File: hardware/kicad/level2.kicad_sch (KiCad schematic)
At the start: 13 parts, among them J1 19V in (switched, fused), J3 motor: A1 A2 B1 B2, J4 to ESP32: STEP DIR EN HALL 3V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, J5 to Hall: 5V GND OUT, J6 to buck: 19V, GND, 5V, M1 NEMA17 (42 x 33.4), U1 BTT TMC2209, U3 ESP32-S3-DevKitC-1 N16R8, U4 A3144 (homing)

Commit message: Perfboard layout: parts on the hole grid, routed wires, wiring picture (perfboard_wiring.png); schematic gets footprints
Co-Authored-By: Claude Opus 5.5 <noreply@anthropic.com>
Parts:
- C1, C2: footprint (none) -> Capacitor_THT:CP_Radial_D8.0mm_P5.00mm
- J1: footprint (none) -> TerminalBlock_Phoenix:TerminalBlock_Phoenix_MKDS-1,5-2-5.08_1x02_P5.08mm_Horizontal
- J3: footprint (none) -> TerminalBlock_Phoenix:TerminalBlock_Phoenix_MKDS-1,5-4-5.08_1x04_P5.08mm_Horizontal
- J4: footprint (none) -> Connector_PinHeader_2.54mm:PinHeader_1x06_P2.54mm_Vertical
- J5: footprint (none) -> Connector_PinHeader_2.54mm:PinHeader_1x03_P2.54mm_Vertical
- J6: footprint (none) -> TerminalBlock_Phoenix:TerminalBlock_Phoenix_MKDS-1,5-3-5.08_1x03_P5.08mm_Horizontal
- R1, R2: footprint (none) -> Resistor_THT:R_Axial_DIN0207_L6.3mm_D2.5mm_P10.16mm_Horizontal
- U1: footprint (none) -> Module:Pololu_Breakout-16_15.2x20.3mm

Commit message: Perfboard: driver turned under J3 (coil wires straight up, A2 A1 B1 B2), J1 + next to J6 19V, C1 above VS; C2 dropped
Co-Authored-By: Claude Opus 5.5 <noreply@anthropic.com>
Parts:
- removed C2: 100uF 50V (opt., at J1), Capacitor_THT:CP_Radial_D8.0mm_P5.00mm, symbol Device:C_Polarized
- J1: value 19V in (switched, fused) -> 19V in: + - left to right
- J3: value motor: A1 A2 B1 B2 -> motor: A2 A1 B1 B2 (left to right on the board)
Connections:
- net +19V_SW: now also J1.2 (Pin_2); no longer J1.1 (Pin_1)
- net GND: now also J1.1 (Pin_1); no longer J1.2 (Pin_2)
- net MOT_A1: now also J3.3 (Pin_3); no longer J3.1 (Pin_1)
- net MOT_A2: now also J3.4 (Pin_4); no longer J3.2 (Pin_2)
- net MOT_B1: now also J3.2 (Pin_2); no longer J3.3 (Pin_3)
- net MOT_B2: now also J3.1 (Pin_1); no longer J3.4 (Pin_4)
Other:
- note added: "Heavy wire (20-22 AWG): 19 V, GND, motor. C1 sits right at U1's VS and the GND next to it."
- note added: "Motor M1: 6-pin socket, pins 1+3 = coil A (red A1, blue A2); pins 4+6 = coil B (green B1, black B2); pins 2, 5 (centre taps) unused. J3 left to right: A2 A1 B1 B2."
- note removed: "Heavy wire (20-22 AWG): 19 V, GND, motor. C1 sits right at U1's VS and the GND next to it; C2 (optional) at J1."
- note removed: "Motor M1: 6-pin socket, pins 1+3 = coil A (red, blue) -> A1, A2; pins 4+6 = coil B (green, black) -> B1, B2; pins 2, 5 (centre taps) unused."
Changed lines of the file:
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@@
 (symbol (lib_id "Connector:Screw_Terminal_01x02") (at 63.5 50.8 0) (unit 1) (exclude_from_sim no) (in_bom yes) (on_board yes) (dnp no)
 (property "Reference" "J1" (at 63.5 48.26 0) (effects (font (size 1.27 1.27))))
-(property "Value" "19V in (switched, fused)" (at 63.5 55.88 0) (effects (font (size 1.27 1.27))))
+(property "Value" "19V in: + - left to right" (at 63.5 55.88 0) (effects (font (size 1.27 1.27))))
 (property "Footprint" "TerminalBlock_Phoenix:TerminalBlock_Phoenix_MKDS-1,5-2-5.08_1x02_P5.08mm_Horizontal" (at 63.5 50.8 0) (effects (font (size 1.27 1.27)) (hide yes)))
 (property "Datasheet" "" (at 63.5 50.8 0) (effects (font (size 1.27 1.27)) (hide yes)))
@@
 (instances (project "piper-watch" (path "/833d4739-1417-5dca-9991-7683c6f341a1/5f72bd5d-36b4-5204-b28a-452f3b5ccb01" (reference "J1") (unit 1)))))
 (wire (pts (xy 58.42 50.8) (xy 55.88 50.8)) (stroke (width 0) (type default)))
-(global_label "+19V_SW" (shape passive) (at 55.88 50.8 180) (fields_autoplaced yes) (effects (font (size 1.27 1.27)) (justify right)) (property "Intersheetrefs" "${INTERSHEET_REFS}" (at 55.88 50.8 0) (effects (font (size 1.27 1.27)) (justify right) (hide yes))))
+(global_label "GND" (shape passive) (at 55.88 50.8 180) (fields_autoplaced yes) (effects (font (size 1.27 1.27)) (justify right)) (property "Intersheetrefs" "${INTERSHEET_REFS}" (at 55.88 50.8 0) (effects (font (size 1.27 1.27)) (justify right) (hide yes))))
 (wire (pts (xy 58.42 53.34) (xy 55.88 53.34)) (stroke (width 0) (type default)))
-(global_label "GND" (shape passive) (at 55.88 53.34 180) (fields_autoplaced yes) (effects (font (size 1.27 1.27)) (justify right)) (property "Intersheetrefs" "${INTERSHEET_REFS}" (at 55.88 53.34 0) (effects (font (size 1.27 1.27)) (justify right) (hide yes))))
+(global_label "+19V_SW" (shape passive) (at 55.88 53.34 180) (fields_autoplaced yes) (effects (font (size 1.27 1.27)) (justify right)) (property "Intersheetrefs" "${INTERSHEET_REFS}" (at 55.88 53.34 0) (effects (font (size 1.27 1.27)) (justify right) (hide yes))))
 (symbol (lib_id "Connector:Screw_Terminal_01x03") (at 63.5 81.28 0) (unit 1) (exclude_from_sim no) (in_bom yes) (on_board yes) (dnp no)
 (property "Reference" "J6" (at 63.5 76.2 0) (effects (font (size 1.27 1.27))))
@@
 (symbol (lib_id "Connector:Screw_Terminal_01x04") (at 63.5 116.84 0) (unit 1) (exclude_from_sim no) (in_bom yes) (on_board yes) (dnp no)
 (property "Reference" "J3" (at 63.5 111.76 0) (effects (font (size 1.27 1.27))))
-(property "Value" "motor: A1 A2 B1 B2" (at 63.5 124.46 0) (effects (font (size 1.27 1.27))))
+(property "Value" "motor: A2 A1 B1 B2 (left to right on the board)" (at 63.5 124.46 0) (effects (font (size 1.27 1.27))))
 (property "Footprint" "TerminalBlock_Phoenix:TerminalBlock_Phoenix_MKDS-1,5-4-5.08_1x04_P5.08mm_Horizontal" (at 63.5 116.84 0) (effects (font (size 1.27 1.27)) (hide yes)))
 (property "Datasheet" "" (at 63.5 116.84 0) (effects (font (size 1.27 1.27)) (hide yes)))
@@
 (instances (project "piper-watch" (path "/833d4739-1417-5dca-9991-7683c6f341a1/5f72bd5d-36b4-5204-b28a-452f3b5ccb01" (reference "J3") (unit 1)))))
 (wire (pts (xy 58.42 114.3) (xy 55.88 114.3)) (stroke (width 0) (type default)))
-(label "MOT_A1" (at 55.88 114.3 180) (effects (font (size 1.27 1.27)) (justify right bottom)))
+(label "MOT_B2" (at 55.88 114.3 180) (effects (font (size 1.27 1.27)) (justify right bottom)))
 (wire (pts (xy 58.42 116.84) (xy 55.88 116.84)) (stroke (width 0) (type default)))
-(label "MOT_A2" (at 55.88 116.84 180) (effects (font (size 1.27 1.27)) (justify right bottom)))
+(label "MOT_B1" (at 55.88 116.84 180) (effects (font (size 1.27 1.27)) (justify right bottom)))
 (wire (pts (xy 58.42 119.38) (xy 55.88 119.38)) (stroke (width 0) (type default)))
-(label "MOT_B1" (at 55.88 119.38 180) (effects (font (size 1.27 1.27)) (justify right bottom)))
+(label "MOT_A1" (at 55.88 119.38 180) (effects (font (size 1.27 1.27)) (justify right bottom)))
 (wire (pts (xy 58.42 121.92) (xy 55.88 121.92)) (stroke (width 0) (type default)))
-(label "MOT_B2" (at 55.88 121.92 180) (effects (font (size 1.27 1.27)) (justify right bottom)))
+(label "MOT_A2" (at 55.88 121.92 180) (effects (font (size 1.27 1.27)) (justify right bottom)))
 (symbol (lib_id "Connector_Generic:Conn_01x06") (at 63.5 160.02 0) (unit 1) (exclude_from_sim no) (in_bom yes) (on_board yes) (dnp no)
 (property "Reference" "J4" (at 63.5 152.4 0) (effects (font (size 1.27 1.27))))
@@
 (wire (pts (xy 124.46 168.91) (xy 124.46 171.45)) (stroke (width 0) (type default)))
 (global_label "GND" (shape passive) (at 124.46 171.45 270) (fields_autoplaced yes) (effects (font (size 1.27 1.27)) (justify right)) (property "Intersheetrefs" "${INTERSHEET_REFS}" (at 124.46 171.45 0) (effects (font (size 1.27 1.27)) (justify right) (hide yes))))
-(symbol (lib_id "Device:C_Polarized") (at 154.94 165.1 0) (unit 1) (exclude_from_sim no) (in_bom yes) (on_board yes) (dnp no)
-(property "Reference" "C2" (at 158.75 163.83 0) (effects (font (size 1.27 1.27)) (justify left)))
-(property "Value" "100uF 50V (opt., at J1)" (at 158.75 166.37 0) (effects (font (size 1.27 1.27)) (justify left)))
-(property "Footprint" "Capacitor_THT:CP_Radial_D8.0mm_P5.00mm" (at 154.94 165.1 0) (effects (font (size 1.27 1.27)) (hide yes)))
-(property "Datasheet" "" (at 154.94 165.1 0) (effects (font (size 1.27 1.27)) (hide yes)))
-(property "Description" "" (at 154.94 165.1 0) (effects (font (size 1.27 1.27)) (hide yes)))
-(pin "1")
-(pin "2")
-(instances (project "piper-watch" (path "/833d4739-1417-5dca-9991-7683c6f341a1/5f72bd5d-36b4-5204-b28a-452f3b5ccb01" (reference "C2") (unit 1)))))
-(wire (pts (xy 154.94 161.29) (xy 154.94 158.75)) (stroke (width 0) (type default)))
-(global_label "+19V_SW" (shape passive) (at 154.94 158.75 90) (fields_autoplaced yes) (effects (font (size 1.27 1.27)) (justify left)) (property "Intersheetrefs" "${INTERSHEET_REFS}" (at 154.94 158.75 0) (effects (font (size 1.27 1.27)) (justify left) (hide yes))))
-(wire (pts (xy 154.94 168.91) (xy 154.94 171.45)) (stroke (width 0) (type default)))
-(global_label "GND" (shape passive) (at 154.94 171.45 270) (fields_autoplaced yes) (effects (font (size 1.27 1.27)) (justify right)) (property "Intersheetrefs" "${INTERSHEET_REFS}" (at 154.94 171.45 0) (effects (font (size 1.27 1.27)) (justify right) (hide yes))))
 (symbol (lib_id "Device:R") (at 185.42 165.1 0) (unit 1) (exclude_from_sim no) (in_bom yes) (on_board yes) (dnp no)
 (property "Reference" "R1" (at 189.23 163.83 0) (effects (font (size 1.27 1.27)) (justify left)))
@@
 (label "MOT_B2" (at 368.3 78.74 180) (effects (font (size 1.27 1.27)) (justify right bottom)))
 (text "PERFBOARD (70 x 50): screw terminals J1 (19 V in), J3 (motor), J6 (buck); pin headers J4 (ESP32), J5 (Hall) with Dupont housings." (exclude_from_sim no) (at 20.32 254 0) (effects (font (size 1.27 1.27)) (justify left bottom)))
-(text "Heavy wire (20-22 AWG): 19 V, GND, motor. C1 sits right at U1's VS and the GND next to it; C2 (optional) at J1." (exclude_from_sim no) (at 20.32 257.81 0) (effects (font (size 1.27 1.27)) (justify left bottom)))
+(text "Heavy wire (20-22 AWG): 19 V, GND, motor. C1 sits right at U1's VS and the GND next to it." (exclude_from_sim no) (at 20.32 257.81 0) (effects (font (size 1.27 1.27)) (justify left bottom)))
 (text "U1 MS1 = MS2 = 3V3: 1/16 microstepping. CLK, TX, RX and DIAG unconnected. Set Vref ~0.7 V before connecting the motor." (exclude_from_sim no) (at 20.32 261.62 0) (effects (font (size 1.27 1.27)) (justify left bottom)))
 (text "R2 (optional) holds EN high (motor off) while the ESP32 boots." (exclude_from_sim no) (at 20.32 265.43 0) (effects (font (size 1.27 1.27)) (justify left bottom)))
-(text "Motor M1: 6-pin socket, pins 1+3 = coil A (red, blue) -> A1, A2; pins 4+6 = coil B (green, black) -> B1, B2; pins 2, 5 (centre taps) unused." (exclude_from_sim no) (at 20.32 269.24 0) (effects (font (size 1.27 1.27)) (justify left bottom)))
+(text "Motor M1: 6-pin socket, pins 1+3 = coil A (red A1, blue A2); pins 4+6 = coil B (green B1, black B2); pins 2, 5 (centre taps) unused. J3 left to right: A2 A1 B1 B2." (exclude_from_sim no) (at 20.32 269.24 0) (effects (font (size 1.27 1.27)) (justify left bottom)))
 (text "U3 (base ESP32-S3) is powered by its USB cable from the Jetson - never also from the buck's 5 V." (exclude_from_sim no) (at 20.32 273.05 0) (effects (font (size 1.27 1.27)) (justify left bottom)))
 (text "Hall U4 (A3144) on the motor bracket's pad: VCC from the 5 V buck, OUT pulled up to 3V3 by R1 (never to 5 V)." (exclude_from_sim no) (at 20.32 276.86 0) (effects (font (size 1.27 1.27)) (justify left bottom)))

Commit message: Perfboard: jacks one hole closer to the edges; C1 100 uF / 35 V as fitted
Co-Authored-By: Claude Opus 5.5 <noreply@anthropic.com>
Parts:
- C1: value 100uF 50V (at U1 VS) -> 100uF 35V (at U1 VS)
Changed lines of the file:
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@@
 (symbol (lib_id "Device:C_Polarized") (at 124.46 165.1 0) (unit 1) (exclude_from_sim no) (in_bom yes) (on_board yes) (dnp no)
 (property "Reference" "C1" (at 128.27 163.83 0) (effects (font (size 1.27 1.27)) (justify left)))
-(property "Value" "100uF 50V (at U1 VS)" (at 128.27 166.37 0) (effects (font (size 1.27 1.27)) (justify left)))
+(property "Value" "100uF 35V (at U1 VS)" (at 128.27 166.37 0) (effects (font (size 1.27 1.27)) (justify left)))
 (property "Footprint" "Capacitor_THT:CP_Radial_D8.0mm_P5.00mm" (at 124.46 165.1 0) (effects (font (size 1.27 1.27)) (hide yes)))
 (property "Datasheet" "" (at 124.46 165.1 0) (effects (font (size 1.27 1.27)) (hide yes)))

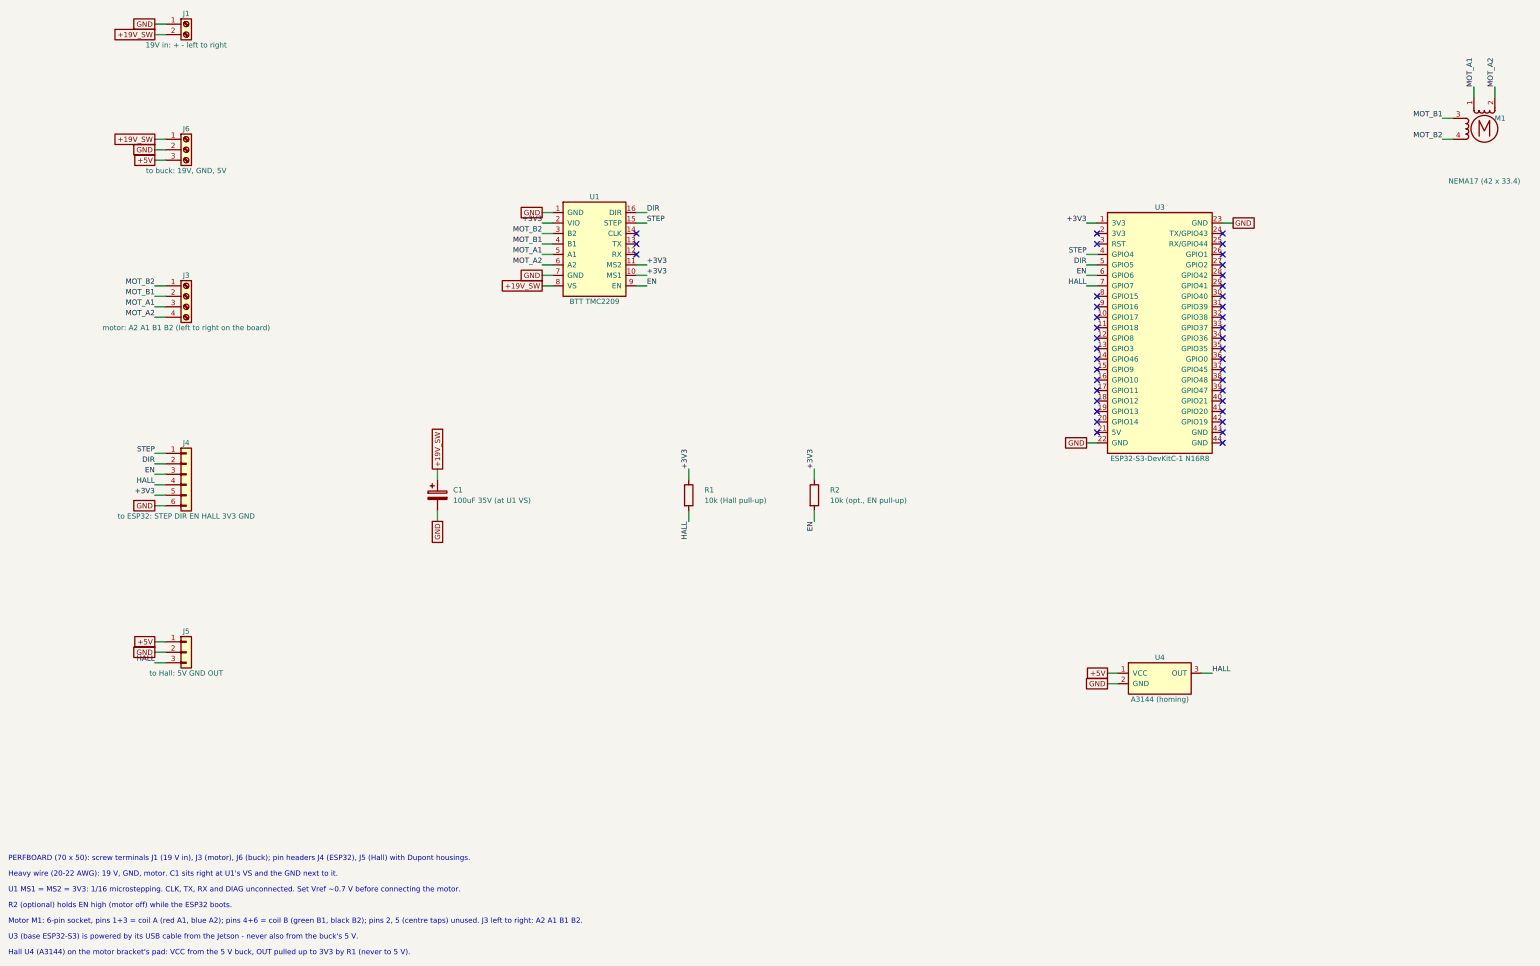
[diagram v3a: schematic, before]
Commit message: One ESP32: the JC4827W543R display's ESP32-S3 runs the pan motor - J4 lead from its P3 (IO15 STEP, IO16 DIR, IO6 EN, IO7 HALL) and P4 (3.3V, GND); R2 now fitted; base DevKit dropped from wiring.md, schematic, READMEs
Co-Authored-By: Claude Opus 5.5 <noreply@anthropic.com>
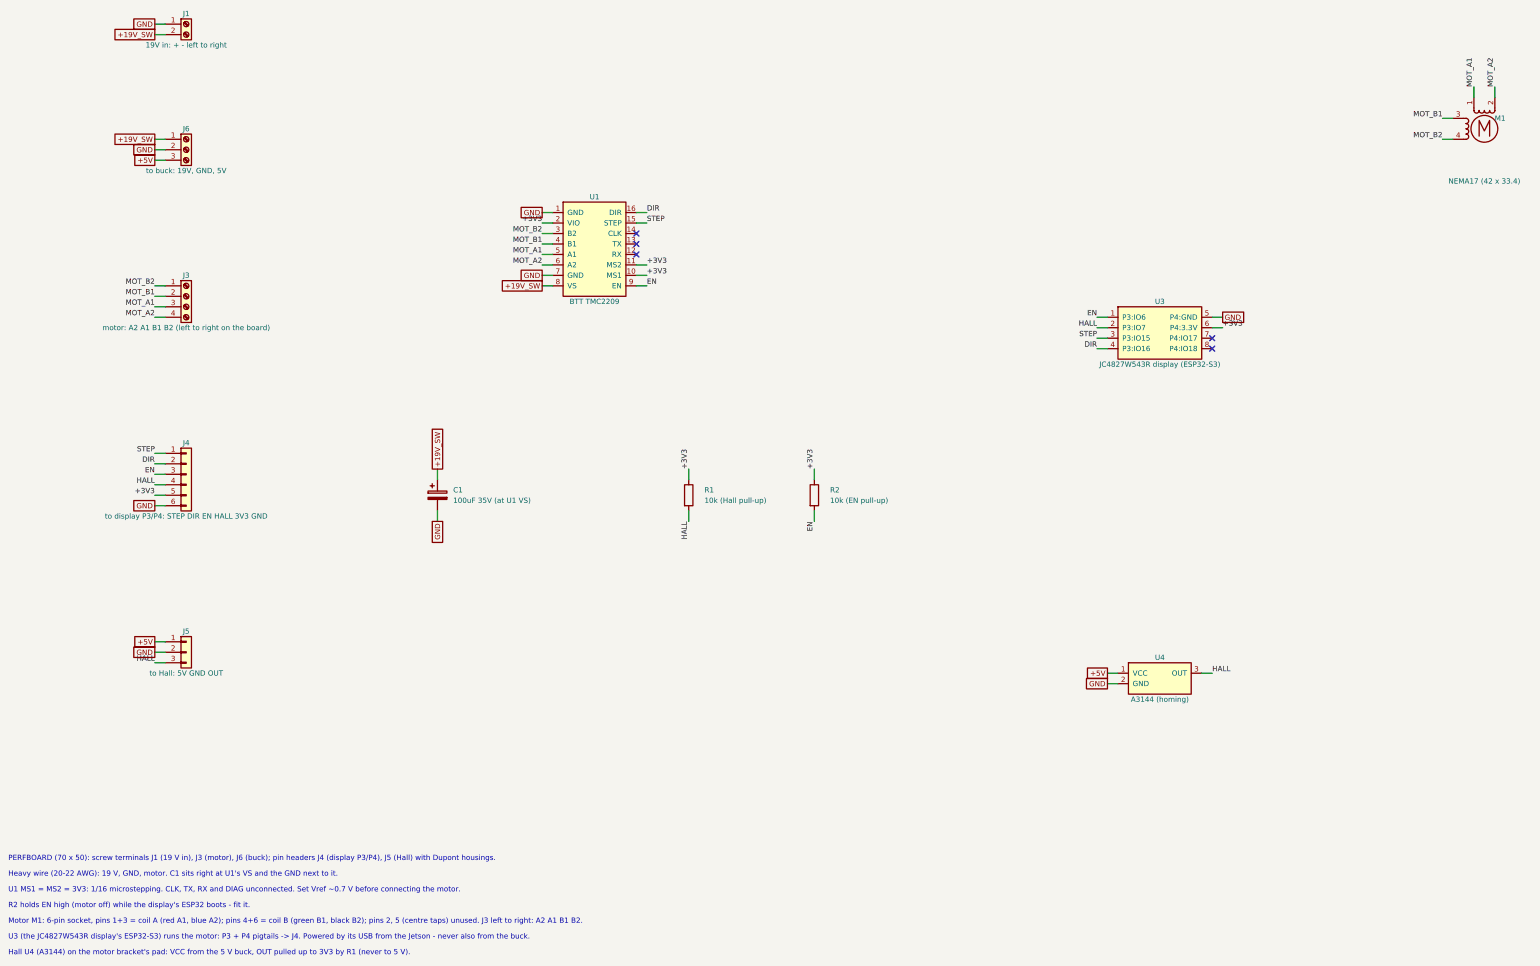
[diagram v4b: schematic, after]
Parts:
- J4: value to ESP32: STEP DIR EN HALL 3V3 GND -> to display P3/P4: STEP DIR EN HALL 3V3 GND
- R2: value 10k (opt., EN pull-up) -> 10k (EN pull-up)
- U3: value ESP32-S3-DevKitC-1 N16R8 -> JC4827W543R display (ESP32-S3); symbol piper-watch:ESP32-S3-DevKitC-1 -> piper-watch:JC4827W543_IO
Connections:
- net +3V3: now also U3.6 (P4:3.3V); no longer U3.1 (3V3)
- net DIR: now also U3.4 (P3:IO16); no longer U3.5 (GPIO5)
- net EN: now also U3.1 (P3:IO6); no longer U3.6 (GPIO6)
- net GND: now also U3.5 (P4:GND); no longer U3.22 (GND), U3.23 (GND)
- net HALL: now also U3.2 (P3:IO7); no longer U3.7 (GPIO7)
- net STEP: now also U3.3 (P3:IO15); no longer U3.4 (GPIO4)
- no-connect marks 40 -> 5
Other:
- note added: "PERFBOARD (70 x 50): screw terminals J1 (19 V in), J3 (motor), J6 (buck); pin headers J4 (display P3/P4), J5 (Hall) with Dupont housings."
- note added: "R2 holds EN high (motor off) while the display's ESP32 boots - fit it."
- note added: "U3 (the JC4827W543R display's ESP32-S3) runs the motor: P3 + P4 pigtails -> J4. Powered by its USB from the Jetson - never also from the buck."
- note removed: "PERFBOARD (70 x 50): screw terminals J1 (19 V in), J3 (motor), J6 (buck); pin headers J4 (ESP32), J5 (Hall) with Dupont housings."
- note removed: "R2 (optional) holds EN high (motor off) while the ESP32 boots."
- note removed: "U3 (base ESP32-S3) is powered by its USB cable from the Jetson - never also from the buck's 5 V."
- title: Level 2: perfboard (TMC2209), base ESP32-S3, Hall sensor, motor -> Level 2: perfboard (TMC2209), the display's ESP32-S3, Hall sensor, motor
